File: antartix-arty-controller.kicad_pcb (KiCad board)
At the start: 4 copper layers, 173.5 x 40 mm, 131 parts, among them IC1 FT2232D, IC2 TPD8S009DSMR, IC3 TPD8S009DSMR, J1 QTE-020-04-L-D-A, J2 614004185023, J3 614004185023, J4 614004185023, J5 WE_629105150521, J6 0022232041, J7 QTE-020-04-L-D-A, J8 685119134923, J9 685119134923, U1 PCT2075GVX, U2 PAC1934T-I_JQ, U3 USB2514B-I_M2, U4 TPS2024DR, U5 TPS2024DR, U6 TPS2024DR, Y1 7C-24.000MBB-T, Y2 MQ-6.000-12-30_30_

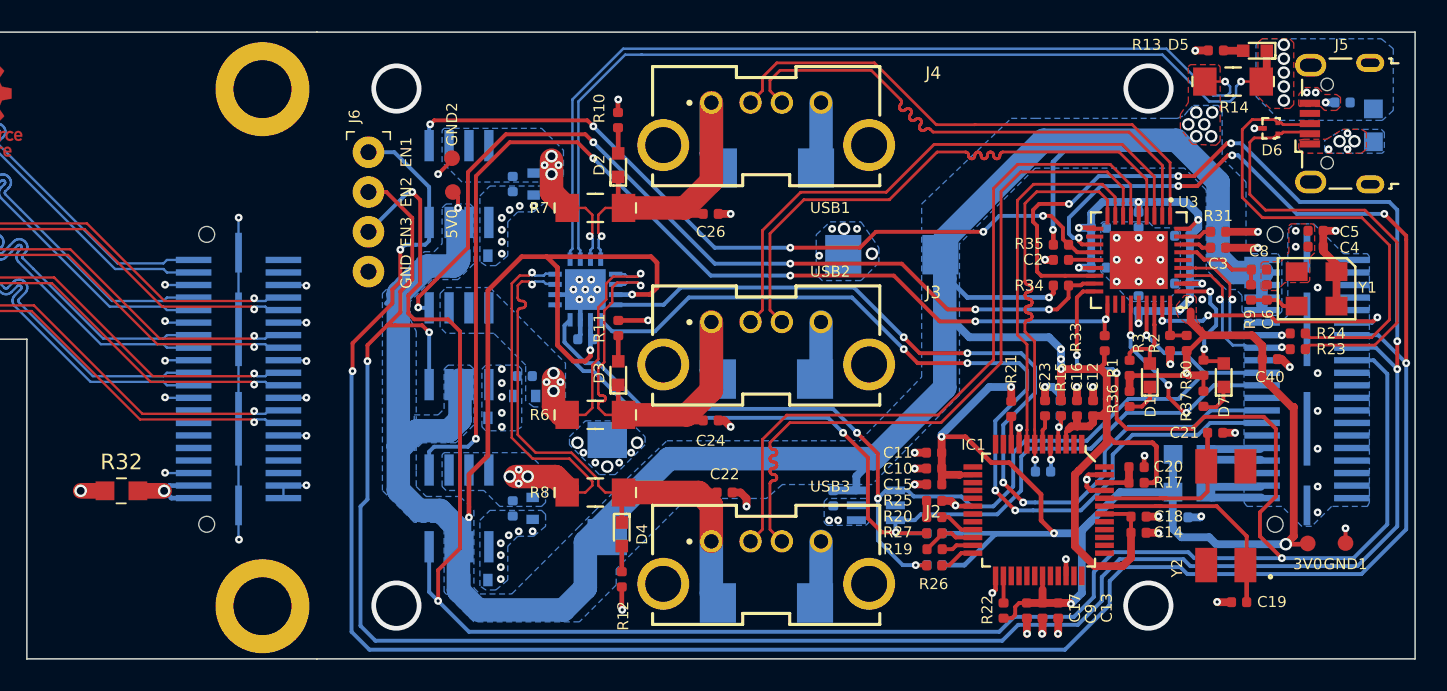
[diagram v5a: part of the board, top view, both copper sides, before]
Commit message: Remove redundant 3V3 traces
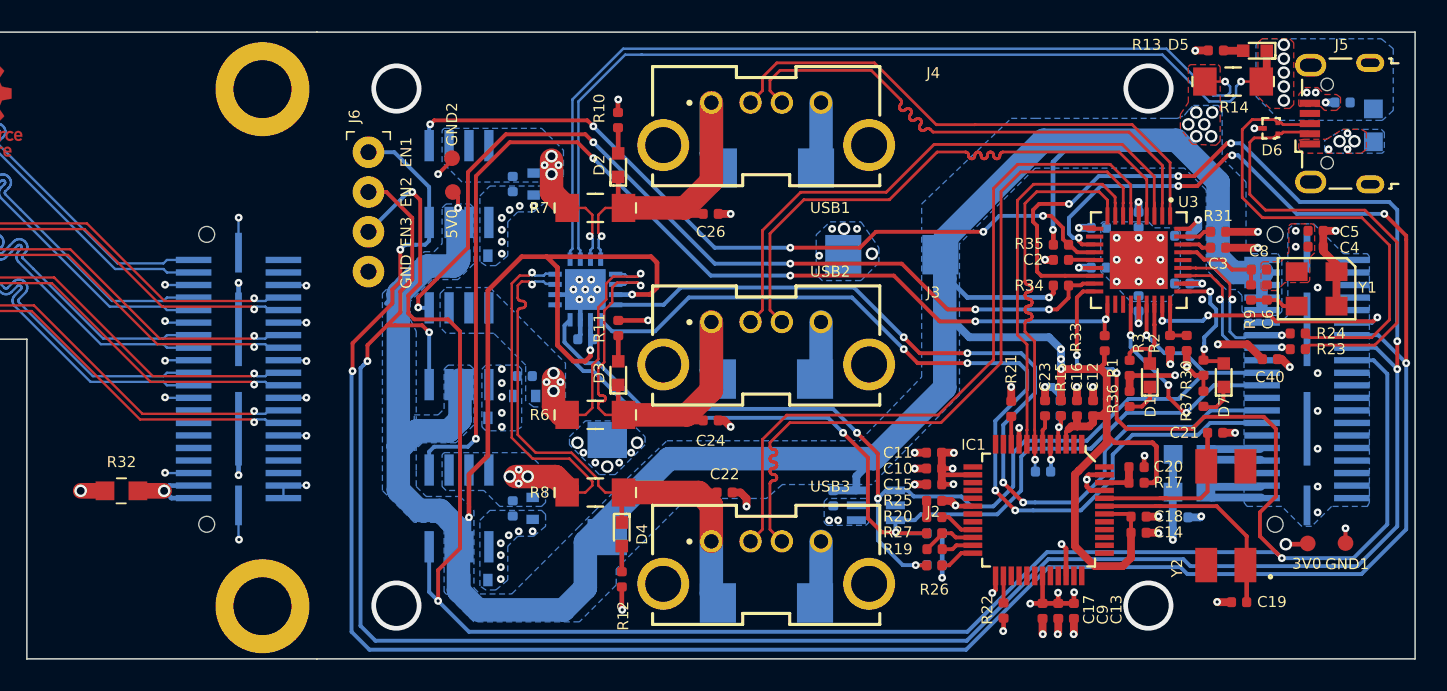
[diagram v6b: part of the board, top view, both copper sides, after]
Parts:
- moved C13 1.00 mm to (216.2, 109.5)
- moved C17 1.00 mm to (214.2, 109.5)
- moved C9 1.00 mm to (215.2, 109.5)
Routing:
- net VCC3V3: track 178.8 -> 89.5 mm, vias 20 -> 26
- net GND: track 126.7 -> 117.6 mm, vias 127 -> 129
- net /USB3_EN: track 146.1 -> 145.2 mm
- net /USB1_EN: track 159.5 -> 158.6 mm
- net /USB2_EN: track 166.2 -> 165.3 mm
- removed copper zone on F.Cu, net VCC3V3

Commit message: Add hierarchical structure
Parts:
- renumbered 3V0 to 3V1, 5V0 to 5V1, C27 to C1, C28 to C10, C29 to C11, C30 to C12, C40 to C13, C31 to C14, C9 to C15, C41 to C16, C10 to C17, C33 to C18, C42 to C19, C1 to C2, C11 to C20, C12 to C21, C37 to C22, C43 to C23, C13 to C24, C14 to C25, C44 to C26, C45 to C27, C15 to C28, C16 to C29, C2 to C3, C47 to C30, C34 to C31, C35 to C33, C46 to C34, C17 to C35, C18 to C36, C38 to C37, C36 to C38, C3 to C4, C48 to C40, C19 to C41, C20 to C42, C21 to C43, C22 to C44, C23 to C45, C24 to C46, C49 to C47, C26 to C48, C4 to C5, C5 to C6, C6 to C7, C7 to C9, D7 to D2, D2 to D3, D3 to D4, D4 to D5, D5 to D6, D6 to D7, J6 to J2, J2 to J3, J5 to J4, J3 to J5, J4 to J6, R24 to R1, R30 to R10, R36 to R11, R37 to R12, R4 to R13, R5 to R14, R7 to R15, R8 to R16, R2 to R17, R3 to R18, R33 to R19, R23 to R2, R34 to R20, R6 to R21, R14 to R22, R35 to R23, R9 to R24, R31 to R25, R15 to R26, R16 to R27, R17 to R28, R18 to R29, R28 to R3, R19 to R30, R20 to R31, R22 to R32, R21 to R33, R25 to R34, R26 to R35, R27 to R36, R32 to R37, R29 to R4, R10 to R5, R11 to R6, R12 to R7, R13 to R8, R1 to R9
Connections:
- net /3V3_RPI renamed /USB/3V3_RPI
- net /3V3_SSD renamed /USB/3V3_SSD
- net /CLKIN renamed /USB/CLKIN
- net /FTDI_RST renamed /USB/FTDI_RST
- net /HS_IND renamed /USB/HS_IND
- net /OC_N1 renamed /USB/OC_N1
- net /OC_N2 renamed /USB/OC_N2
- net /OC_N3 renamed /USB/OC_N3
- net /RESET_N renamed /USB/RESET_N
- net /SCL_FTDI renamed /USB/SCL_FTDI
- net /SDA_FTDI renamed /USB/SDA_FTDI
- net /SLOW_~ALERT renamed /USB/SLOW_~ALERT
- net /SUSP_IND renamed /USB/SUSP_IND
- net /USB1_D_N renamed /USB/USB1_D_N
- net /USB1_D_P renamed /USB/USB1_D_P
- net /USB1_EN renamed /USB/USB1_EN
- net /USB2_D_N renamed /USB/USB2_D_N
- net /USB2_D_P renamed /USB/USB2_D_P
- net /USB2_EN renamed /USB/USB2_EN
- net /USB3_D_N renamed /USB/USB3_D_N
- net /USB3_D_P renamed /USB/USB3_D_P
- net /USB3_EN renamed /USB/USB3_EN
- net /USB_D_CON_N renamed /USB/USB_D_CON_N
- net /USB_D_CON_P renamed /USB/USB_D_CON_P
- net /USB_D_FTDI_N renamed /USB/USB_D_FTDI_N
- net /USB_D_FTDI_P renamed /USB/USB_D_FTDI_P
- net /WP_FTDI renamed /USB/WP_FTDI
- net /~PWRDN renamed /USB/~PWRDN

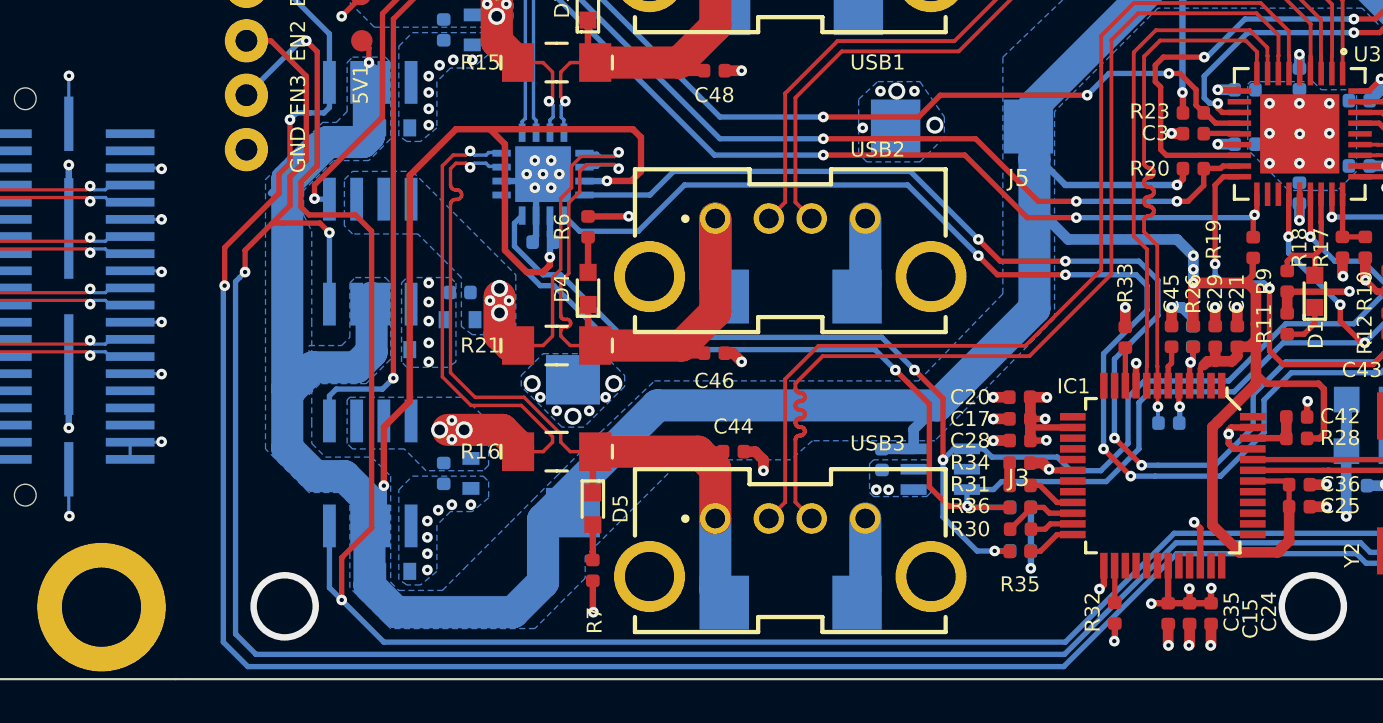
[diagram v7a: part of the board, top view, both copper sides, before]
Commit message: Connect UART(GPIO14 & GPIO15)to BDBUS of FTDI
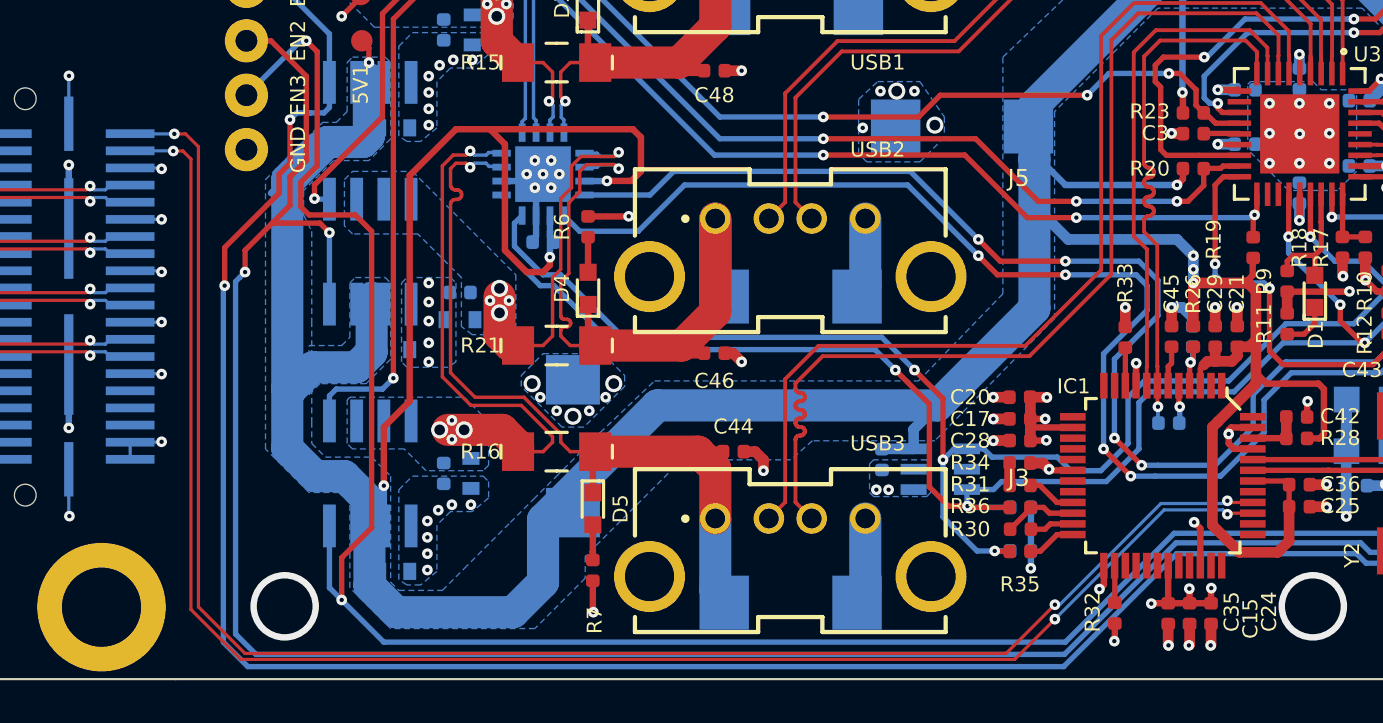
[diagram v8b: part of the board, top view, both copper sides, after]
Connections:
- net /USB/3V3_RPI renamed /antartix usb adapter/3V3_RPI
- net /USB/3V3_SSD renamed /antartix usb adapter/3V3_SSD
- net /USB/CLKIN renamed /antartix usb adapter/CLKIN
- net /USB/FTDI_RST renamed /antartix usb adapter/FTDI_RST
- net /USB/HS_IND renamed /antartix usb adapter/HS_IND
- net /USB/OC_N1 renamed /antartix usb adapter/OC_N1
- net /USB/OC_N2 renamed /antartix usb adapter/OC_N2
- net /USB/OC_N3 renamed /antartix usb adapter/OC_N3
- net /USB/RESET_N renamed /antartix usb adapter/RESET_N
- net /USB/SCL_FTDI renamed /antartix usb adapter/SCL_FTDI
- net /USB/SDA_FTDI renamed /antartix usb adapter/SDA_FTDI
- net /USB/SLOW_~ALERT renamed /antartix usb adapter/SLOW_~ALERT
- net /USB/SUSP_IND renamed /antartix usb adapter/SUSP_IND
- net /USB/USB1_D_N renamed /antartix usb adapter/USB1_D_N
- net /USB/USB1_D_P renamed /antartix usb adapter/USB1_D_P
- net /USB/USB1_EN renamed /antartix usb adapter/USB1_EN
- net /USB/USB2_D_N renamed /antartix usb adapter/USB2_D_N
- net /USB/USB2_D_P renamed /antartix usb adapter/USB2_D_P
- net /USB/USB2_EN renamed /antartix usb adapter/USB2_EN
- net /USB/USB3_D_N renamed /antartix usb adapter/USB3_D_N
- net /USB/USB3_D_P renamed /antartix usb adapter/USB3_D_P
- net /USB/USB3_EN renamed /antartix usb adapter/USB3_EN
- net /USB/USB_D_CON_N renamed /antartix usb adapter/USB_D_CON_N
- net /USB/USB_D_CON_P renamed /antartix usb adapter/USB_D_CON_P
- net /USB/USB_D_FTDI_N renamed /antartix usb adapter/USB_D_FTDI_N
- net /USB/USB_D_FTDI_P renamed /antartix usb adapter/USB_D_FTDI_P
- net /USB/WP_FTDI renamed /antartix usb adapter/WP_FTDI
- net /USB/~PWRDN renamed /antartix usb adapter/~PWRDN
- IC1 pad 39: Net-(IC1-Pad39) -> RXD0
- IC1 pad 40: Net-(IC1-Pad40) -> TXD0
- J7 pad 2: GPIO14 -> TXD0
- J7 pad 4: GPIO15 -> RXD0
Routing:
- net TXD0: track 0.00 -> 78.0 mm, vias 0 -> 3
- net RXD0: track 0.00 -> 77.5 mm, vias 0 -> 3
